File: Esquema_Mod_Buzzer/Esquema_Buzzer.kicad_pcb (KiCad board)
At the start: 2 copper layers, 0 parts

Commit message: [ADD]
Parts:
- added BZ1: Buzzer, Buzzer_Beeper:Buzzer_12x9.5RM7.6, F.Cu at (151.9, 31.5)
- added C1: 100uf, Capacitor_SMD:CP_Elec_3x5.3, F.Cu at (148.7, 22.6)
- added C2: 22uF, Capacitor_SMD:CP_Elec_3x5.3, F.Cu at (134.4, 23.3)
- added D1: SS34, Diode_SMD:D_2114_3652Metric_Pad1.85x3.75mm_HandSolder, F.Cu at (144.5, 28.2)
- added J1: Conn_01x02_Pin, Connector_AMASS2:AMASS_XT30PW-M_1x02_P2.50mm_Horizontal, F.Cu at (129.7, 25.5)
- added J2: Conn_01x03_Pin, Connector_PinHeader_1.00mm:PinHeader_1x03_P1.00mm_Horizontal, F.Cu at (120.0, 39.0)
- added L1: 10uH, Inductor_SMD:L_7.3x7.3_H4.5, F.Cu at (137.1, 30.5)
- added Q1: BC337, Package_TO_SOT_THT:TO-92_Inline, F.Cu at (135.8, 37.1)
- added R1: 1k, Resistor_THT:R_Axial_DIN0204_L3.6mm_D1.6mm_P5.08mm_Horizontal, F.Cu at (144.3, 35.1)
- added R2: 10k, Resistor_SMD:R_0201_0603Metric, F.Cu at (144.4, 22.7)
- added R3: 390, Resistor_SMD:R_0201_0603Metric, F.Cu at (142.7, 22.7)
- added U1: PC817, Package_DIP:DIP-4_W7.62mm, F.Cu at (123.2, 36.7)
- added U2: MT3608, Package_TO_SOT_SMD:SOT-23-6, F.Cu at (139.5, 23.1)
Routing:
- net (no net): track 22.5 -> 0.00 mm, vias 14 -> 0
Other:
- board text removed: "+"
- board text removed: "-"
- board text removed: "Anode"
- board text removed: "B"
- board text removed: "C"
- board text removed: "Cathode"
- board text removed: "E"
- board text removed: "J1+"
- board text removed: "M1"
- board text removed: "Q1"
- board text removed: "R1 + BZ1"
- board text removed: "U1"
- board text removed: "U2+"
- board text removed: "U2-"

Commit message: [ADD] some projects
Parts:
- added G***: LOGO, LOGO, F.Cu at (170.2, 95.9)
- moved R1 76.5 mm to (156.0, 110.7), turned to 90 degrees
- moved R2 73.2 mm to (160.5, 94.1), turned to 0 degrees
- moved BZ1 72.9 mm to (164.0, 103.4)
- moved D1 71.5 mm to (161.5, 97.6), turned to 180 degrees
- moved C2 71.4 mm to (150.2, 92.9)
- moved J1 71.4 mm to (145.4, 95.1)
- moved J2 71.4 mm to (135.8, 108.6)
- moved L1 71.4 mm to (152.8, 100.1)
- moved Q1 71.4 mm to (151.6, 106.8)
- moved U1 71.4 mm to (138.9, 106.3)
- moved U2 71.4 mm to (155.2, 92.7)
- moved R3 71.1 mm to (159.2, 91.9)
- moved C1 70.9 mm to (163.8, 91.9), turned to 90 degrees
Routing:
- net GND: track 0.00 -> 56.3 mm
- net Net-(BZ1-+): track 0.00 -> 25.9 mm
- net Net-(J1-Pin_2): track 0.00 -> 25.4 mm
- net Net-(BZ1--): track 0.00 -> 15.9 mm
- net Net-(D1-A): track 0.00 -> 9.40 mm
- net Net-(U2-FB): track 0.00 -> 6.25 mm
- net Net-(Q1-B): track 0.00 -> 5.38 mm
- net Net-(J2-Pin_3): track 0.00 -> 3.31 mm
- net Net-(J2-Pin_1): track 0.00 -> 3.30 mm
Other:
- board outline added: 40 x 30 mm
- board text added: "Buzzer"

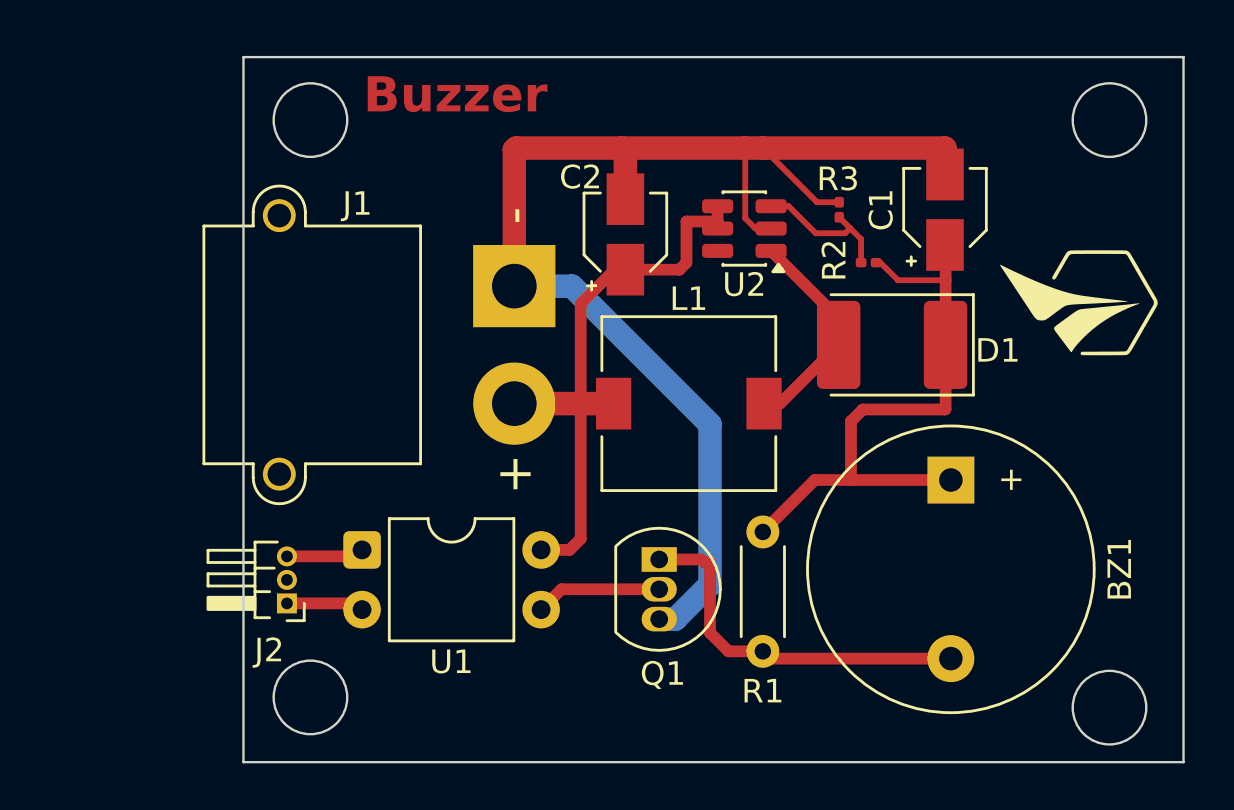
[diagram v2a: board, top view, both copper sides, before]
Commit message: [UP] Upgrade Buzzer
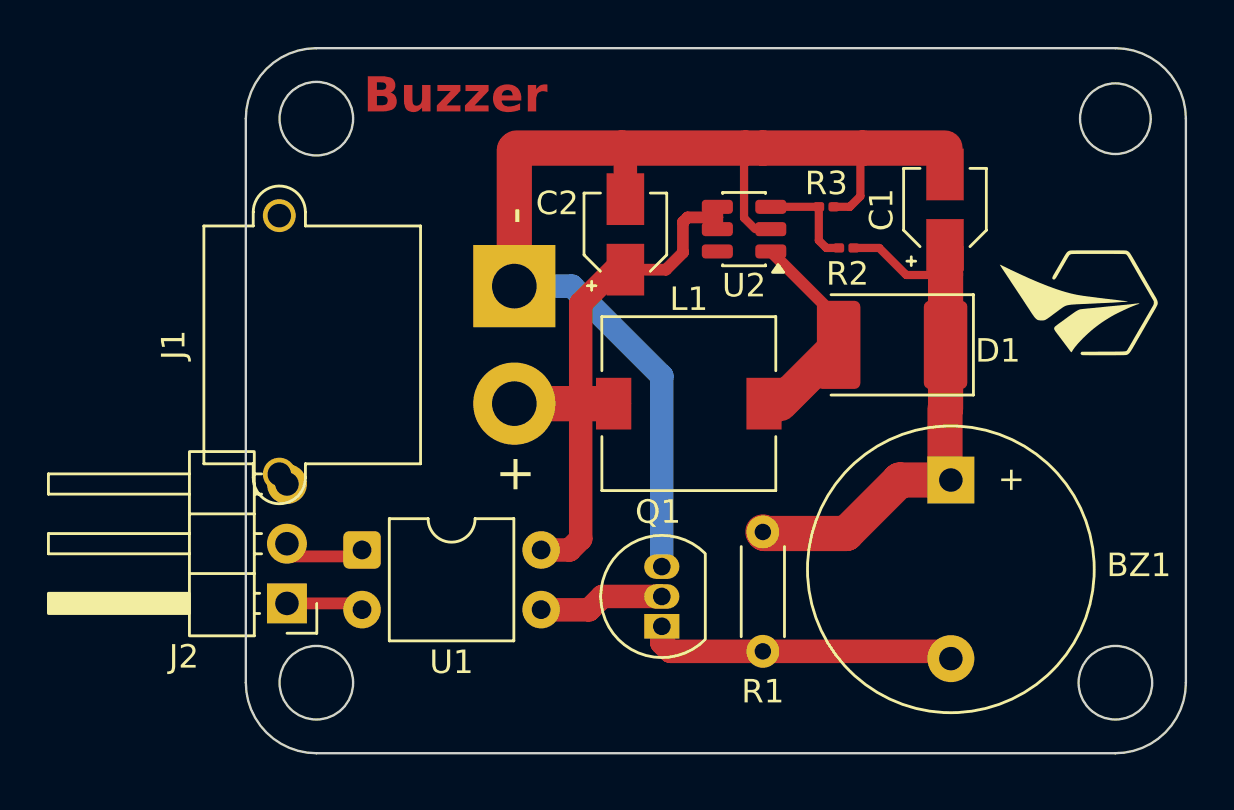
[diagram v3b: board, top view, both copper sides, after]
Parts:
- J1: footprint Connector_AMASS2:AMASS_XT30PW-M_1x02_P2.50mm_Horizontal -> Amass:AMASS_XT30PW-M_1x02_P2.50mm_Horizontal
- J2: footprint Connector_PinHeader_1.00mm:PinHeader_1x03_P1.00mm_Horizontal -> Connector_PinHeader_2.54mm:PinHeader_1x03_P2.54mm_Horizontal
- moved Q1 2.85 mm to (151.7, 109.6), turned to 90 degrees
- moved R2 1.14 mm to (159.6, 93.5)
- moved R3 0.56 mm to (158.7, 91.8), turned to 180 degrees
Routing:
- net GND: track 56.3 -> 51.2 mm
- net Net-(BZ1--): track 15.9 -> 13.3 mm
- net Net-(BZ1-+): track 25.9 -> 23.9 mm
- net Net-(U2-FB): track 6.25 -> 4.46 mm
- net Net-(D1-A): track 9.40 -> 10.5 mm
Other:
- outline, holes or cut-outs redrawn
